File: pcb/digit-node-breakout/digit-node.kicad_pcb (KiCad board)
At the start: 2 copper layers, 20 parts, among them J1 Conn_01x09_Male, J2 STM32_SWD, Q1 PZT2222A, Q2 PZT2222A, U1 STM32F030F4Px

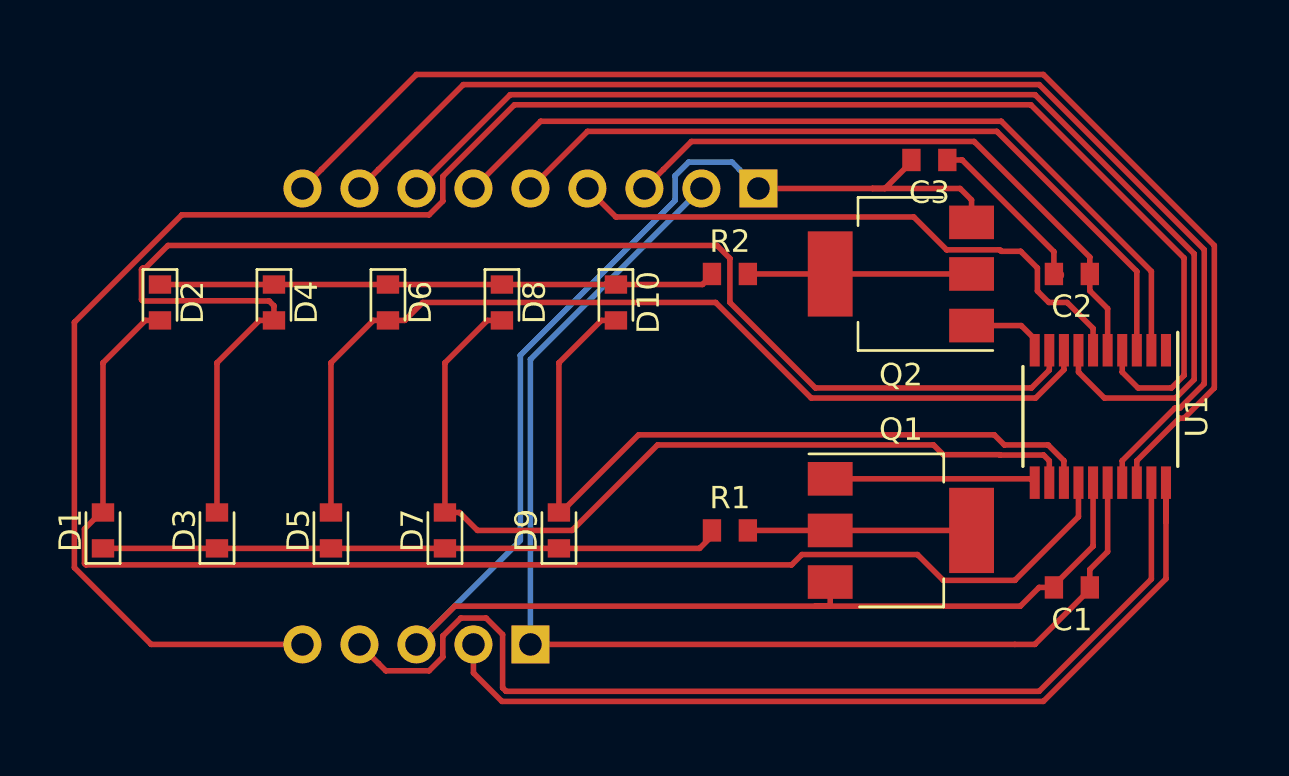
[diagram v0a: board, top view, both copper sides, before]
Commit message: Ground planes
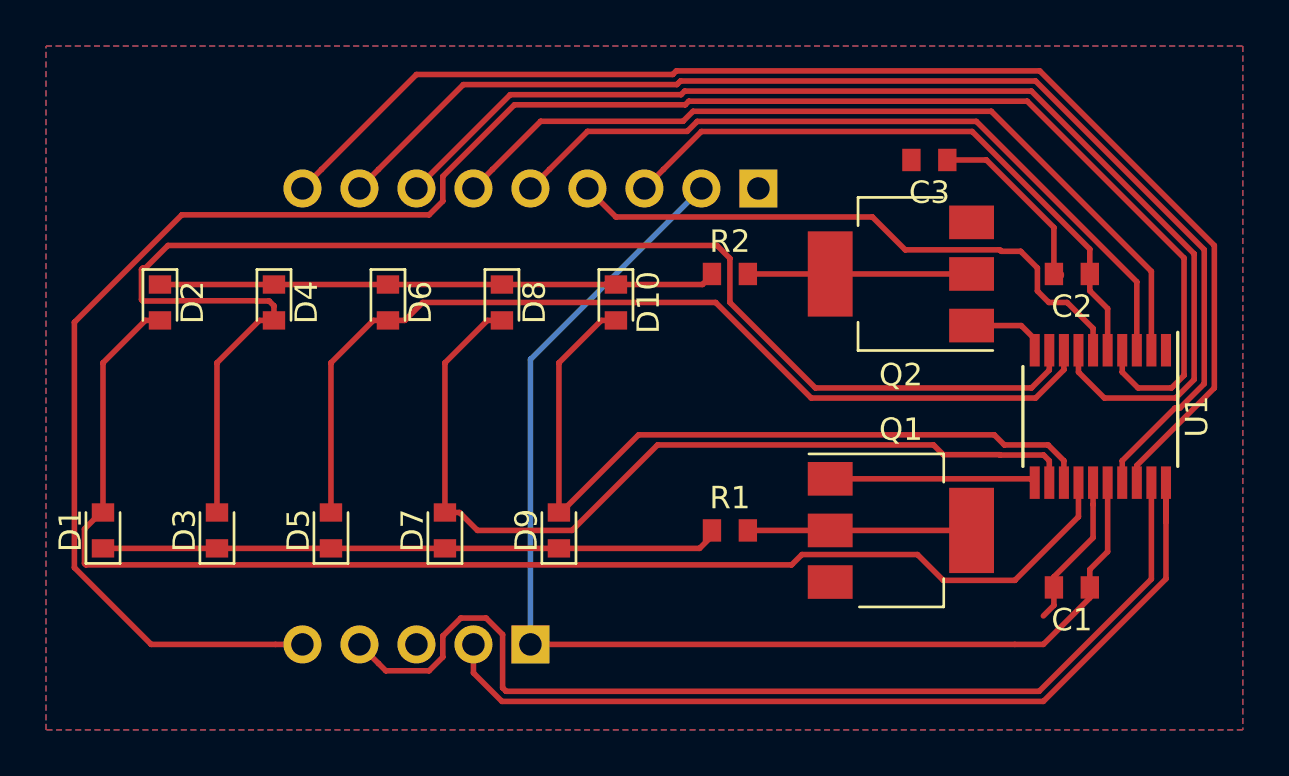
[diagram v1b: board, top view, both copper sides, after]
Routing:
- net GND: track 79.7 -> 7.04 mm
- net Net-(C2-Pad2): track 7.52 -> 8.16 mm
- net VDDA: track 27.4 -> 28.0 mm
- added copper zone on B.Cu, net GND
- added copper zone on F.Cu, net GND

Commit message: Board outline
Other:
- board outline added: 53.3 x 30.5 mm
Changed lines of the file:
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@@
   (general
     (thickness 1.6)
-    (drawings 0)
+    (drawings 4)
     (tracks 216)
     (zones 0)
@@
     )
   )
+  (gr_line (start 99.06 101.6) (end 99.06 71.12) (layer Edge.Cuts) (width 0.1))
+  (gr_line (start 152.4 101.6) (end 99.06 101.6) (layer Edge.Cuts) (width 0.1))
+  (gr_line (start 152.4 71.12) (end 152.4 101.6) (layer Edge.Cuts) (width 0.1))
+  (gr_line (start 99.06 71.12) (end 152.4 71.12) (layer Edge.Cuts) (width 0.1))
   (segment (start 128.79 92.91) (end 128.79 92.71) (width 0.25) (layer F.Cu) (net 1) (status 30))
   (segment (start 128.19 93.51) (end 128.79 92.91) (width 0.25) (layer F.Cu) (net 1) (status 20))
@@
   (segment (start 139.049999 89.334999) (end 138.615 88.9) (width 0.25) (layer F.Cu) (net 7))
   (segment (start 138.615 88.9) (end 126.315002 88.9) (width 0.25) (layer F.Cu) (net 7))
+  (segment (start 143.520011 89.350011) (end 141.585013 89.350011) (width 0.25) (layer F.Cu) (net 7))
+  (segment (start 143.775 90.58) (end 143.775 89.605) (width 0.25) (layer F.Cu) (net 7) (status 10))
+  (segment (start 143.775 89.605) (end 143.520011 89.350011) (width 0.25) (layer F.Cu) (net 7))
   (segment (start 121.92 85.24) (end 123.81 83.35) (width 0.25) (layer F.Cu) (net 8))
   (segment (start 123.81 83.35) (end 124.46 83.35) (width 0.25) (layer F.Cu) (net 8) (status 20))
@@
   (segment (start 141.321402 88.449989) (end 141.771413 88.9) (width 0.25) (layer F.Cu) (net 8))
   (segment (start 121.92 91.91) (end 122.01 91.91) (width 0.25) (layer F.Cu) (net 8) (status 30))
-  (segment (start 143.520011 89.350011) (end 141.585013 89.350011) (width 0.25) (layer F.Cu) (net 7))
-  (segment (start 143.775 90.58) (end 143.775 89.605) (width 0.25) (layer F.Cu) (net 7) (status 10))
-  (segment (start 143.775 89.605) (end 143.520011 89.350011) (width 0.25) (layer F.Cu) (net 7))
   (segment (start 144.425 89.605) (end 143.72 88.9) (width 0.25) (layer F.Cu) (net 8))
   (segment (start 143.72 88.9) (end 141.771413 88.9) (width 0.25) (layer F.Cu) (net 8))
